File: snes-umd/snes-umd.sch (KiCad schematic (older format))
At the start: 2 parts

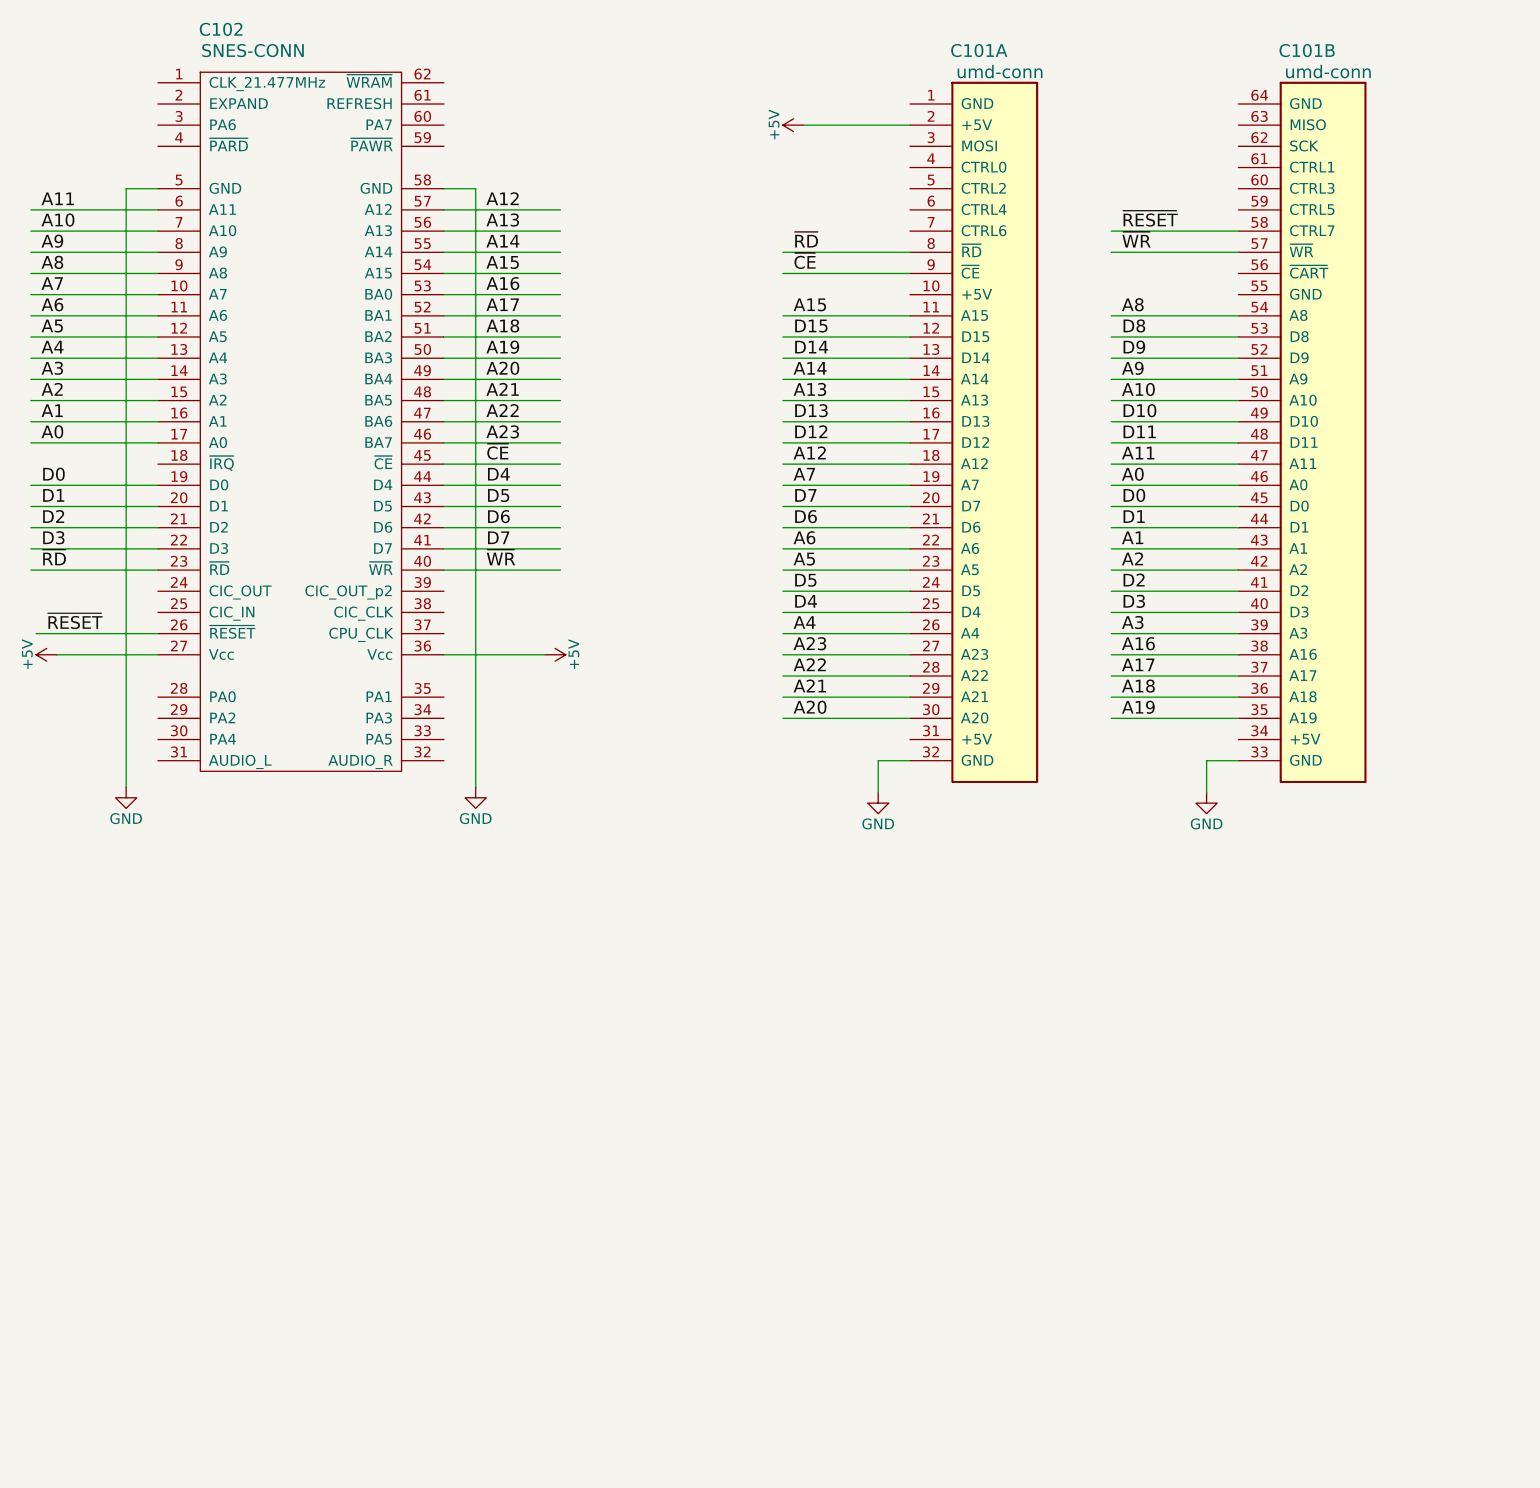
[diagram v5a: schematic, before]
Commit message: fixed the backwards nintendo pin numbering scheme
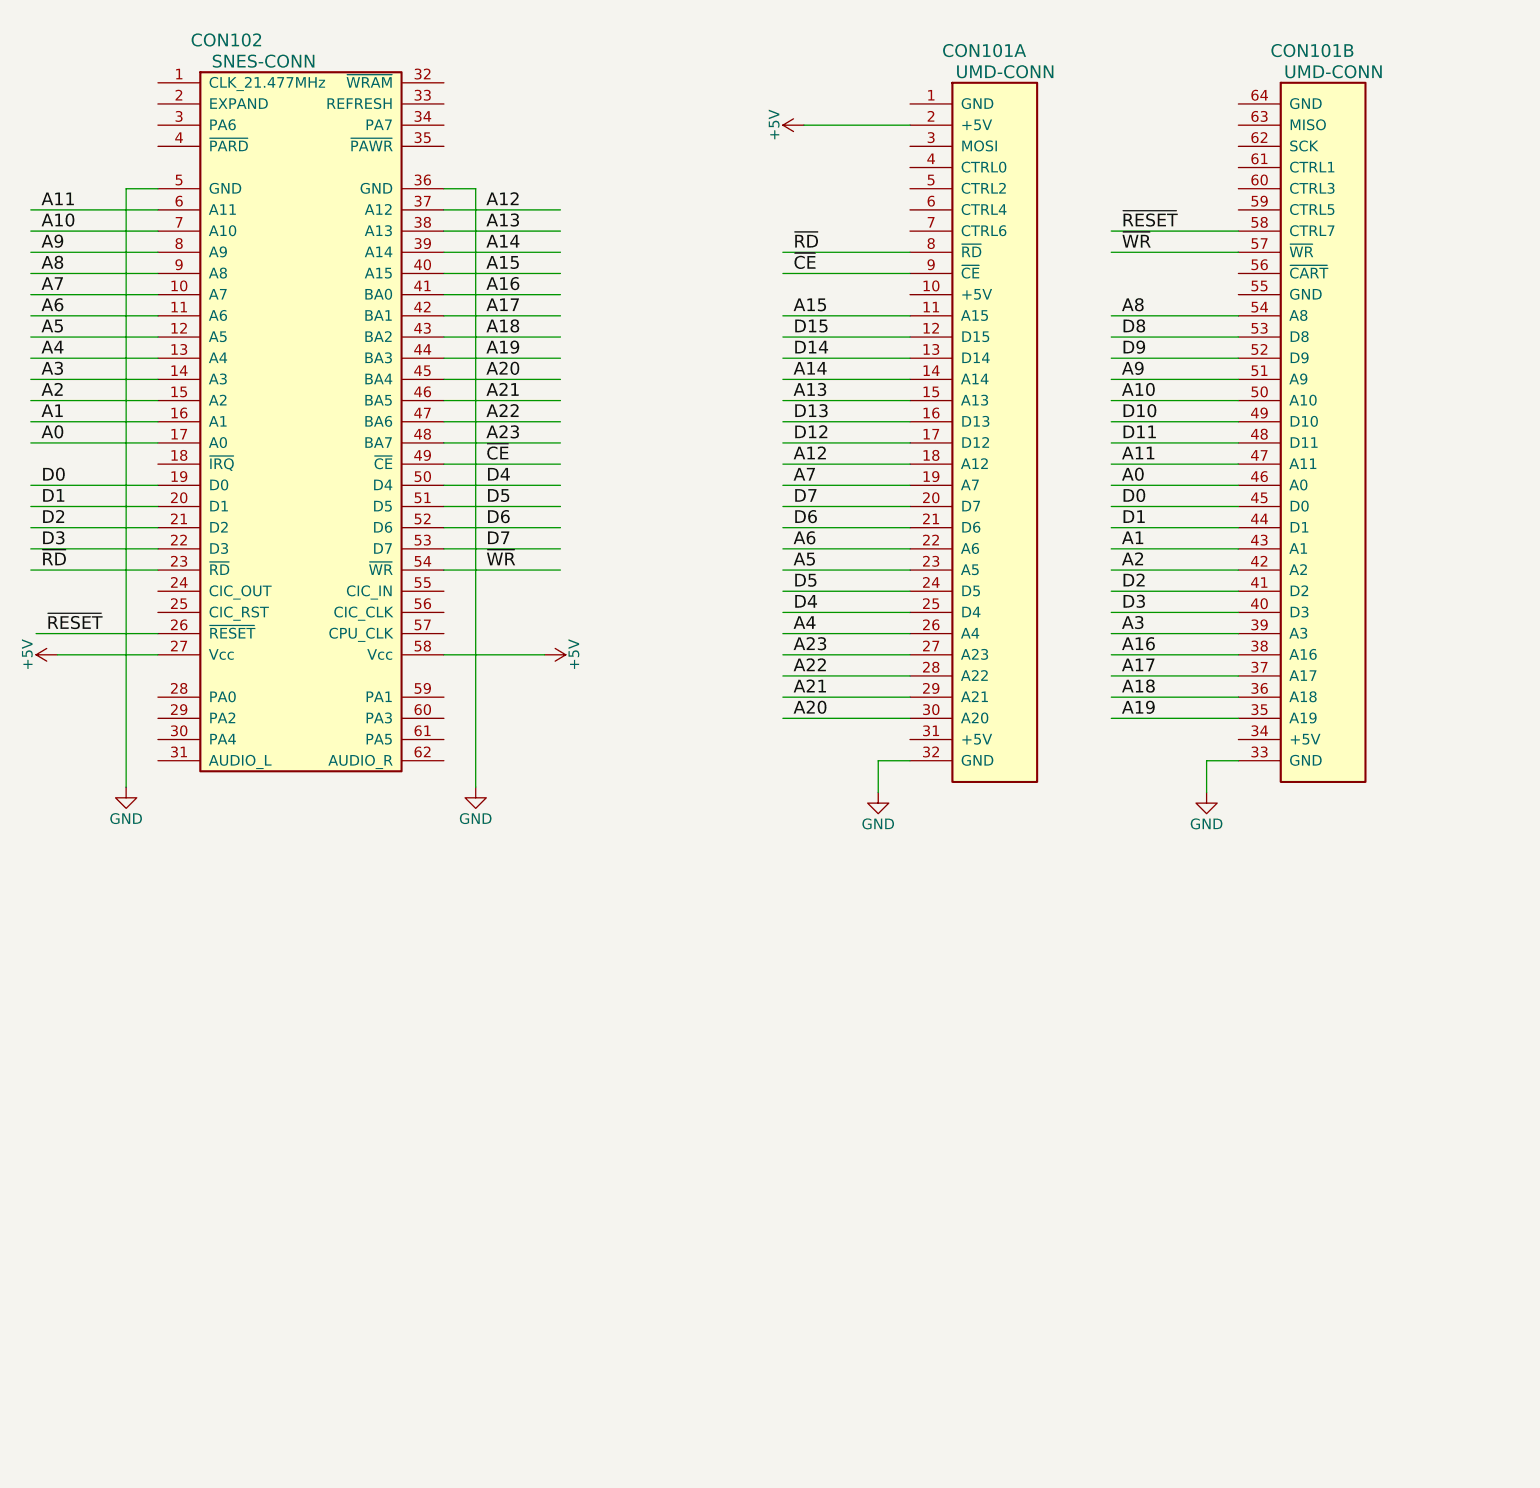
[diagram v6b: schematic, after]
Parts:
- removed C101: umd-conn, db-thparts:UMD-CONN-DIP64, symbol umd-conn
- removed C102: SNES-CONN, db-thparts:SNES-CONN-EXP, symbol SNES-CONN-RESCUE-snes-umd
- added CON101: UMD-CONN, db-thparts:UMD-CONN-DIP64, symbol UMD-CONN
- added CON102: SNES-CONN, symbol SNES-CONN
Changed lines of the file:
@@
 LIBS:db-vgparts
 LIBS:power
-LIBS:device
-LIBS:switches
-LIBS:relays
-LIBS:motors
-LIBS:transistors
-LIBS:conn
-LIBS:linear
-LIBS:regul
-LIBS:74xx
-LIBS:cmos4000
-LIBS:adc-dac
-LIBS:memory
-LIBS:xilinx
-LIBS:microcontrollers
-LIBS:dsp
-LIBS:microchip
-LIBS:analog_switches
-LIBS:motorola
-LIBS:texas
-LIBS:intel
-LIBS:audio
-LIBS:interface
-LIBS:digital-audio
-LIBS:philips
-LIBS:display
-LIBS:cypress
-LIBS:siliconi
-LIBS:opto
-LIBS:atmel
-LIBS:contrib
-LIBS:valves
 LIBS:snes-umd-cache
 EELAYER 25 0
@@
 Comment4 ""
 $EndDescr
-$Comp
-L umd-conn C101
-U 1 1 5A5E3E42
-P 6500 5550
-F 0 "C101" H 6625 9000 60  0000 C CNN
-F 1 "umd-conn" H 6725 8900 60  0000 C CNN
-F 2 "db-thparts:UMD-CONN-DIP64" H 6850 6100 60  0001 C CNN
-F 3 "" H 6850 6100 60  0001 C CNN
-	1    6500 5550
-	1    0    0    -1
-$EndComp
-$Comp
-L umd-conn C101
-U 2 1 5A5E3EE5
-P 8050 5550
-F 0 "C101" H 8175 9000 60  0000 C CNN
-F 1 "umd-conn" H 8275 8900 60  0000 C CNN
-F 2 "" H 8400 6100 60  0001 C CNN
-F 3 "" H 8400 6100 60  0001 C CNN
-	2    8050 5550
-	1    0    0    -1
-$EndComp
 $Comp
 L GND #PWR01
@@
 Text Label 7300 3050 0    60   ~ 0
 ~WR
-$Comp
-L SNES-CONN-RESCUE-snes-umd C102
-U 1 1 5A62100A
-P 2950 5500
-F 0 "C102" H 3050 9000 60  0000 C CNN
-F 1 "SNES-CONN" H 3200 8900 60  0000 C CNN
-F 2 "db-thparts:SNES-CONN-EXP" H 3150 5400 60  0001 C CNN
-F 3 "" H 3150 5400 60  0001 C CNN
-	1    2950 5500
-	1    0    0    -1
-$EndComp
 Wire Wire Line
 	7850 2950 7250 2950
@@
 Wire Wire Line
 	7700 5450 7700 5600
+$Comp
+L SNES-CONN CON102
+U 1 1 5A716175
+P 2950 2200
+F 0 "CON102" H 3075 2350 60  0000 C CNN
+F 1 "SNES-CONN" H 3250 2250 60  0000 C CNN
+F 2 "" H 3150 -1200 60  0001 C CNN
+F 3 "" H 3150 -1200 60  0001 C CNN
+	1    2950 2200
+	1    0    0    -1
+$EndComp
+$Comp
+L UMD-CONN CON101
+U 1 1 5A7163E6
+P 6500 5550
+F 0 "CON101" H 6650 9000 60  0000 C CNN
+F 1 "UMD-CONN" H 6750 8900 60  0000 C CNN
+F 2 "db-thparts:UMD-CONN-DIP64" H 7225 9200 60  0001 C CNN
+F 3 "" H 6850 6100 60  0001 C CNN
+	1    6500 5550
+	1    0    0    -1
+$EndComp
+$Comp
+L UMD-CONN CON101
+U 2 1 5A7164A1
+P 8050 5550
+F 0 "CON101" H 8200 9000 60  0000 C CNN
+F 1 "UMD-CONN" H 8300 8900 60  0000 C CNN
+F 2 "db-thparts:UMD-CONN-DIP64" H 8775 9200 60  0001 C CNN
+F 3 "" H 8400 6100 60  0001 C CNN
+	2    8050 5550
+	1    0    0    -1
+$EndComp
 $EndSCHEMATC

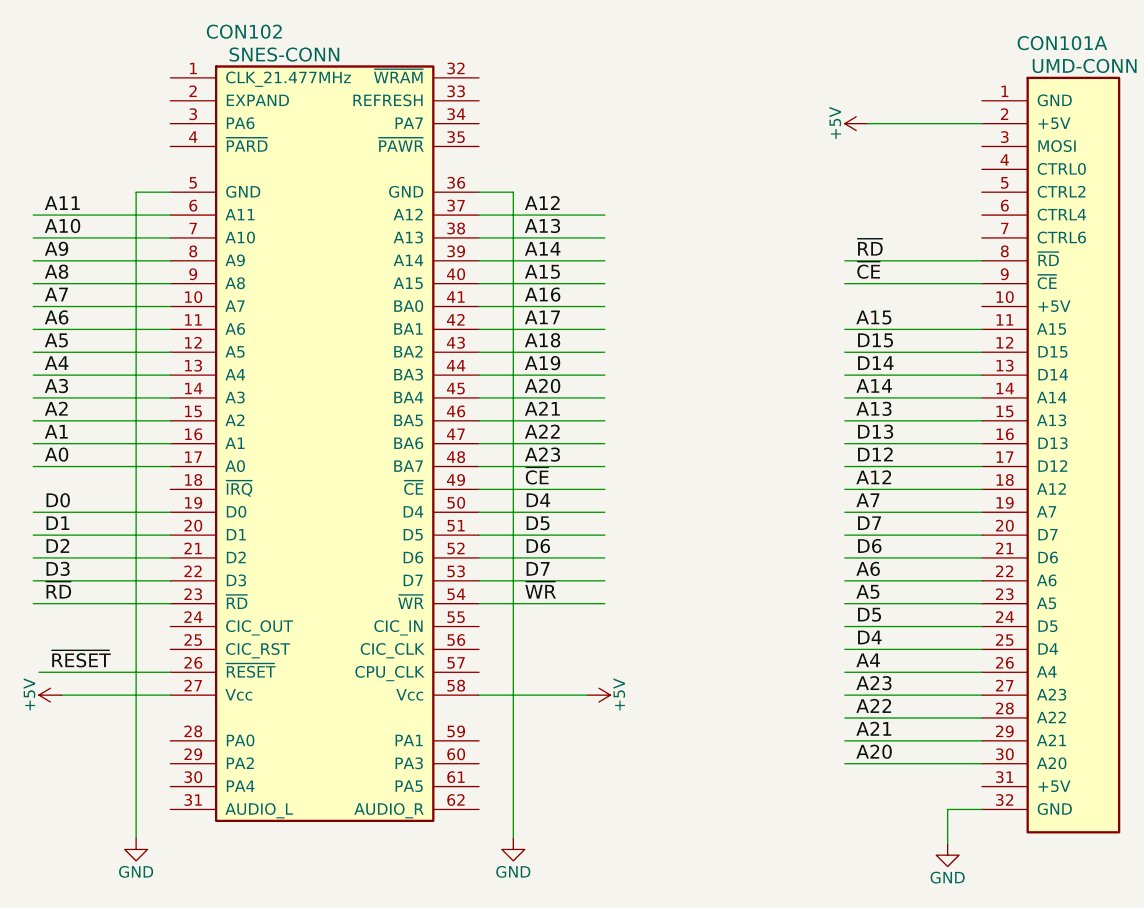
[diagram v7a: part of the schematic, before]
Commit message: release 0.1 snes-umd to fab
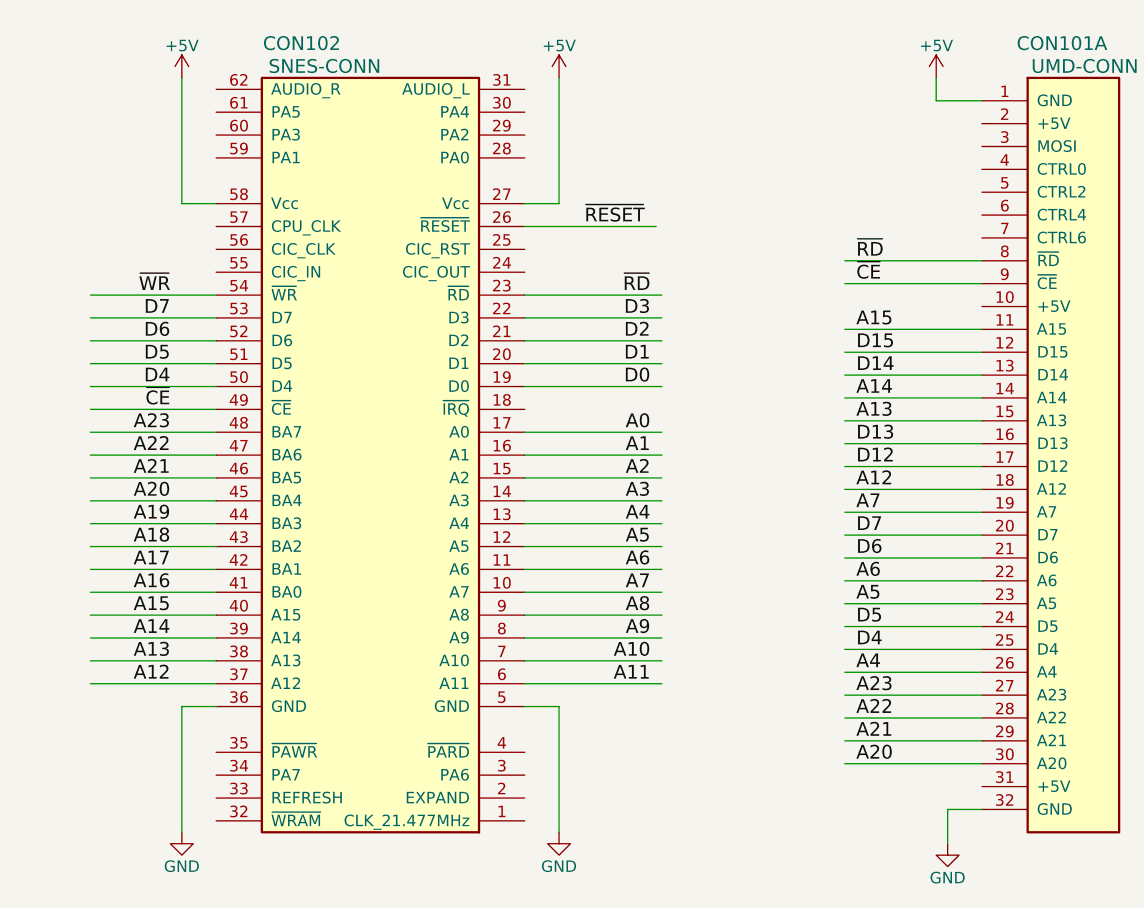
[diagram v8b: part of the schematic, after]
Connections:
- wire segments 91 -> 94
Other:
- moved on the sheet: CON102
